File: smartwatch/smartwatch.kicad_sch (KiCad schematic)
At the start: 2 parts, among them U1 ESP32-S3-WROOM-1, U2 AMS1117-3.3

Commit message: finished pcb and sch
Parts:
- removed U1: ESP32-S3-WROOM-1, Espressif:ESP32-WROVER-E, symbol Espressif:ESP32-S3-WROOM-1
- removed U2: AMS1117-3.3, Package_TO_SOT_SMD:SOT-223-3_TabPin2, symbol Regulator_Linear:AMS1117-3.3
- added BOOT/FLASH1: BOOT/FLASH, Button_Switch_SMD:SW_SPST_Omron_B3FS-100xP, symbol Switch:SW_Push
- added C1, C2, C5, C6: 100nF, Capacitor_SMD:C_0805_2012Metric_Pad1.18x1.45mm_HandSolder, symbol Device:C
- added C11, C12: Polarized_10uF, Capacitor_Tantalum_SMD:CP_EIA-2012-12_Kemet-R_Pad1.30x1.05mm_HandSolder, symbol Device:C_Polarized
- added C3, C4, C8: 10nF, Capacitor_SMD:C_0805_2012Metric_Pad1.18x1.45mm_HandSolder, symbol Device:C
- added C5, C7: 0.1uF, Capacitor_SMD:C_0805_2012Metric_Pad1.18x1.45mm_HandSolder, symbol Device:C
- added C6: 2.2nF, Capacitor_SMD:C_0805_2012Metric_Pad1.18x1.45mm_HandSolder, symbol Device:C
- added GREEN1: CHARGED, LED_SMD:LED_0805_2012Metric_Pad1.15x1.40mm_HandSolder, symbol Device:LED
- added J1: BAT_CON, Connector_Wire_SMD:Wire_Pad_1x02, symbol Connector_Generic:Conn_01x02
- added J2: DC_CON, Connector_Wire_SMD:Wire_Pad_1x02, symbol Connector_Generic:Conn_01x02
- added J3: PROG_INT, Connector_Wire_SMD:Wire_Pad_1x02, symbol Connector_Generic:Conn_01x02
- added J4: I2C Touch, Connector_Wire_SMD:Wire_Pad_1x02, symbol Connector_Generic:Conn_01x02
- added J5: SPI Display, Connector_Wire_SMD:Wire_Pad_1x03, symbol Connector_Generic:Conn_01x03
- added J6: Power, Connector_Wire_SMD:Wire_Pad_1x02, symbol Connector_Generic:Conn_01x02
- added J7: Micro_SD_Card, Connector_Card:microSD_HC_Hirose_DM3D-SF, symbol Connector:Micro_SD_Card
- added R1: 2.2KΩ, Resistor_SMD:R_0805_2012Metric_Pad1.20x1.40mm_HandSolder, symbol Device:R
- added R2, R3: 470Ω, Resistor_SMD:R_0805_2012Metric_Pad1.20x1.40mm_HandSolder, symbol Device:R
- added RED1: CHARGING, LED_SMD:LED_0805_2012Metric_Pad1.15x1.40mm_HandSolder, symbol Device:LED
- added RST1: RST, Button_Switch_SMD:SW_SPST_Omron_B3FS-100xP, symbol Switch:SW_Push
- added U1: ESP32-WROVER-E, Espressif:ESP32-WROVER-E, symbol Espressif:ESP32-WROVER-E
- added U2: MCP73831-5-OT, Package_TO_SOT_SMD:SOT-23-5, symbol Battery_Management:MCP73831-5-OT
- added U3: TLV1117-33, Package_TO_SOT_SMD:SOT-223-3_TabPin2, symbol Regulator_Linear:TLV1117-33
- added U3: MPU-6050, Sensor_Motion:InvenSense_QFN-24_4x4mm_P0.5mm, symbol Sensor_Motion:MPU-6050
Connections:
- new net: R2.2, RED1.2 (A)
- new net: C7.1, U3.10 (REGOUT)
- new net: C6.1, U3.20 (CPOUT)
- new net: GREEN1.1 (K), R3.1
- new net: R1.1, U2.5 (PROG)
- new net 3V3: C2.2, C4.2, C5.1, J6.2 (Pin_2), J7.4 (VDD), U1.2 (3V3), U3.13 (VDD), U3.2 (VO)
- new net BAT_VDD: C1.2, C11.1, C3.2, J1.2 (Pin_2), U2.3 (V_{BAT}), U3.3 (VI)
- new net DC_5V_IN: C12.1, J2.2 (Pin_2), R2.1, U2.4 (V_{DD})
- new net EN: C6.2, RST1.1, U1.3 (EN/CHIP_PU)
- new net GND: BOOT/FLASH1.2, C1.1, C11.2, C12.2, C2.1, C3.1, C4.1, C5.1, C5.2, C6.1, C6.2, C7.2, C8.2, J1.1 (Pin_1), J2.1 (Pin_1), J6.1 (Pin_1), J7.6 (VSS), R1.2, R3.2, RST1.2, U1.1 (GND), U1.15 (GND), U1.38 (GND), U1.39 (GND_THERMAL), U2.2 (V_{SS}), U3.1 (CLKIN), U3.1 (GND), U3.11 (FSYNC), U3.18 (GND)
- new net IO0: BOOT/FLASH1.1, C5.2, U1.25 (GPIO0/BOOT/ADC2_CH1)
- new net IO2: U1.24 (ADC2_CH2/GPIO2)
- new net MCP_1: GREEN1.2 (A), RED1.1 (K), U2.1 (STAT)
- new net MPU_AD0: U3.9 (AD0)
- new net MPU_INT: U3.12 (INT)
- new net MPU_SCL: U1.9 (32K_XN/GPIO33/ADC1_CH5), U3.23 (SCL)
- new net MPU_SDA: U1.8 (32K_XP/GPIO32/ADC1_CH4), U3.24 (SDA)
- new net MPU_VLOGIC: C8.1, U3.8 (VLOGIC)
- new net MPU_XCL: U3.7 (AUX_CL)
- new net MPU_XDA: U3.6 (AUX_DA)
- new net RX: J3.1 (Pin_1), U1.34 (U0RXD/GPIO3)
- new net SCR_MISO: J5.2 (Pin_2), U1.31 (GPIO19)
- new net SCR_MOSI: J5.3 (Pin_3), U1.37 (GPIO23)
- new net SCR_SCLK: J5.1 (Pin_1), U1.30 (GPIO18)
- new net SD_MISO: J7.7 (DAT0), U1.14 (MTDI/GPIO12/ADC2_CH5)
- new net SD_MOSI: J7.3 (CMD), U1.16 (MTCK/GPIO13/ADC2_CH4)
- new net SD_SCLK: J7.5 (CLK), U1.13 (MTMS/GPIO14/ADC2_CH6)
- new net SD_SS: J7.2 (DAT3/CD), U1.23 (MTDO/GPIO15/ADC2_CH3)
- new net TOUCH_SCL: J4.1 (Pin_1), U1.36 (GPIO22)
- new net TOUCH_SDA: J4.2 (Pin_2), U1.33 (GPIO21)
- new net TX: J3.2 (Pin_2), U1.35 (U0TXD/GPIO1)
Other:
- note added: "Battery and Charging"
- note added: "HSPI SPI Interface"
- note added: "Main Board"
- note added: "Motion Unit"
- note added: "Power Regulator"
- note added: "Programming Interface"
- note added: "Storage"
- note added: "Switch Buttons"
- note added: "Touch Screen"
- note added: "VSPI (DEFAULT) SPI Interface and default I2C"

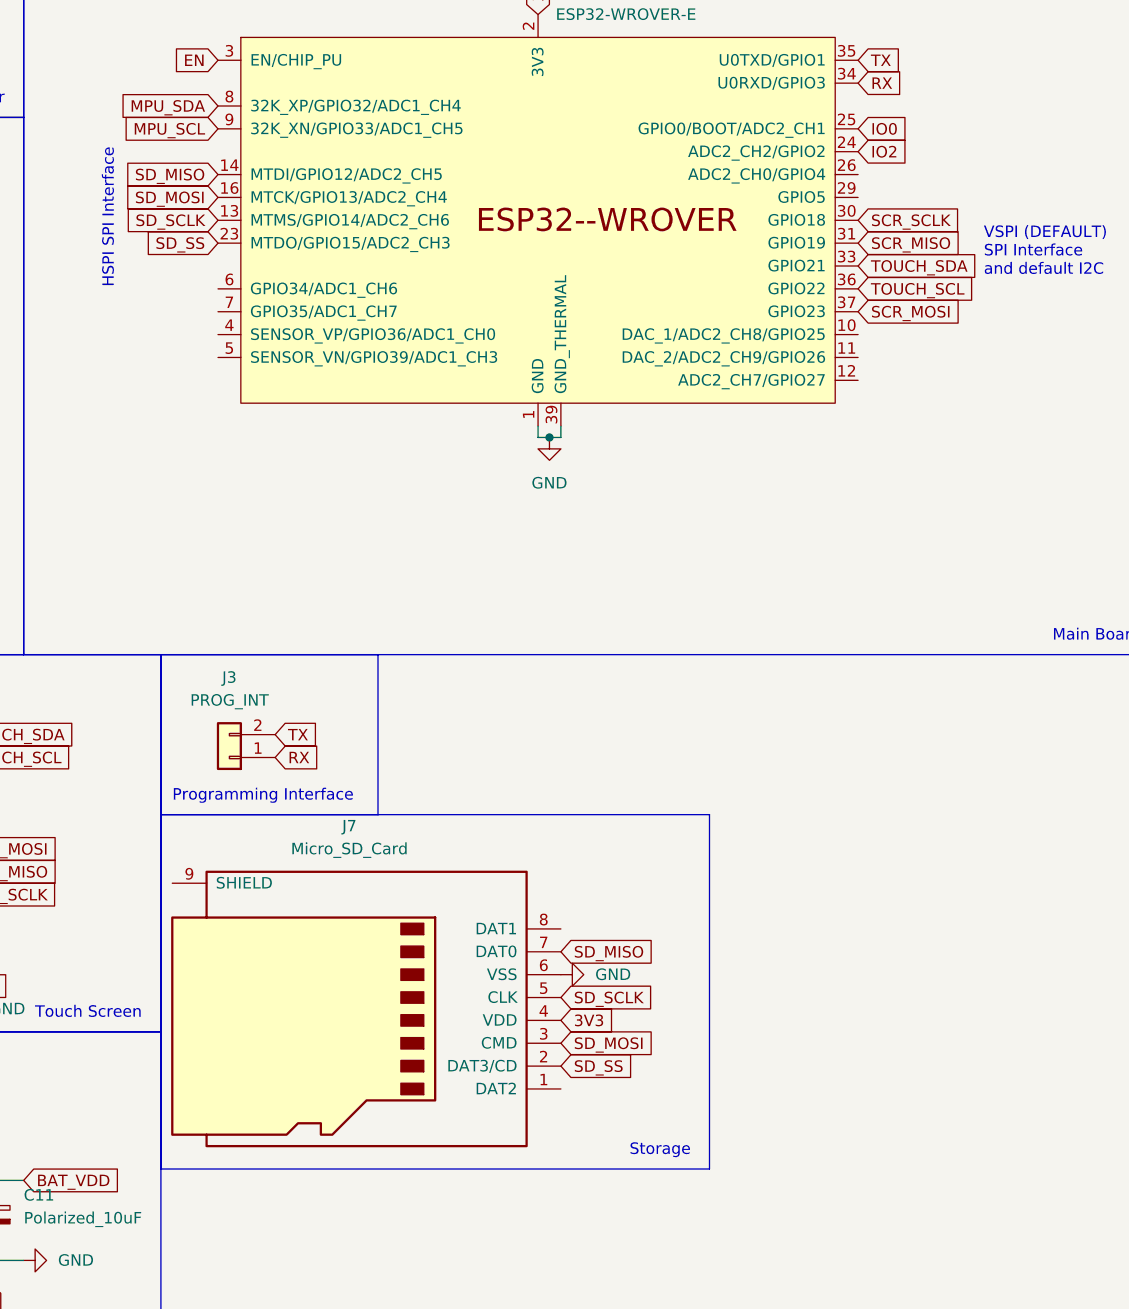
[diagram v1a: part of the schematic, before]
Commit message: added button
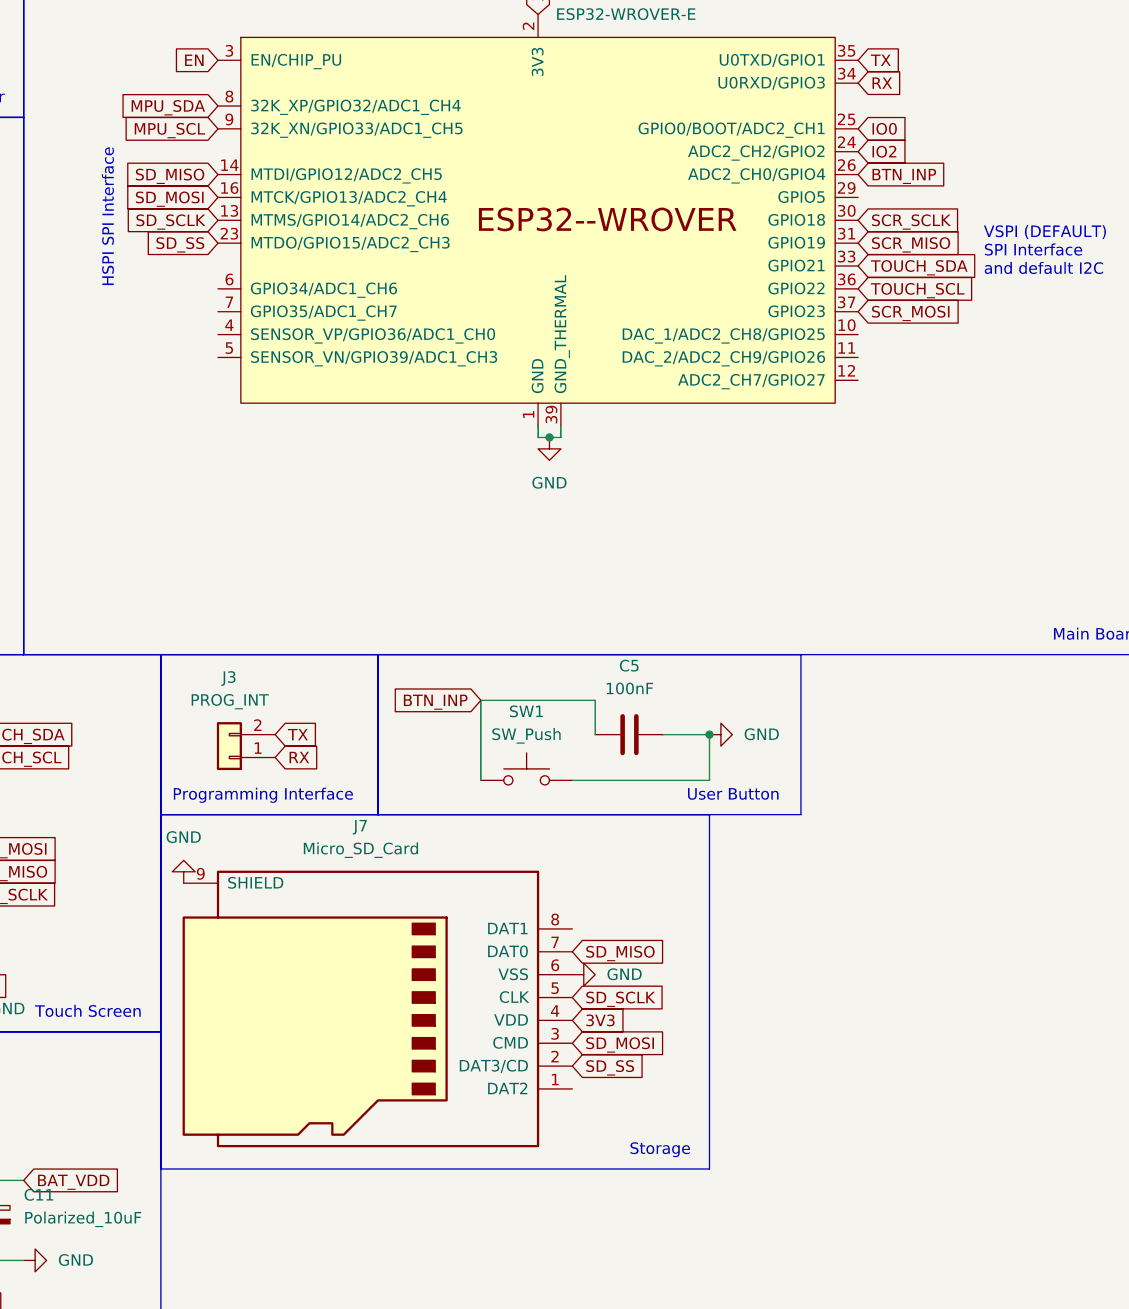
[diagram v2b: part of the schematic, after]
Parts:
- added C5: 100nF, Capacitor_SMD:C_0805_2012Metric_Pad1.18x1.45mm_HandSolder, symbol Device:C
- added SW1: SW_Push, Side_Button:Wurth_Elektronik_436331045822, symbol Switch:SW_Push
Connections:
- net GND: now also J7.9 (SHIELD), C5.1, SW1.2
- net BTN_INP: now reaches U1.26 (ADC2_CH0/GPIO4)
- net BTN_INP: now also C5.2, SW1.1
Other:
- note added: "User Button"
- moved on the sheet: J7
